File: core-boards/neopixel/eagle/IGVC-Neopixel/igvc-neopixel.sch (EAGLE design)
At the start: 21 parts, among them IC1 RT8289, IC2 ATMEGA8, X1 MSTBA2

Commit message: 11/17/19 I fixed the issues
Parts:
- removed ICSP: ICSP, pinhead:PINHD-2X3
- added ICSP1: ICSP, pinhead:PINHD-2X3
- added R5: 1M, SmartPrj:R-EU_R0603
- added R6: 27R, SmartPrj:R-EU_R0603
- added R7: 330, rcl:R-US_R0603
- added Y1: 16MHz, SmartPrj:RESONATORMU
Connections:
- new net N$1: JP1.2, R7.2
- new net XT1: R5.1, R6.2, Y1.3
- new net XT1R: IC2.XTAL1, R6.1
- new net XT2: IC2.XTAL2, R5.2, Y1.1
- net +5V: now also ICSP1.2; no longer ICSP.2
- net GND: now also ICSP1.6, Y1.2; no longer ICSP.6
- net LED_DATA: now also R7.1; no longer JP1.2
- net MISO: now also ICSP1.1; no longer ICSP.1
- net MOSI: now also ICSP1.4; no longer ICSP.4
- net RESET: now also ICSP1.5; no longer ICSP.5
- net SCK: now also ICSP1.3; no longer ICSP.3
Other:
- note added: "MISO"
- note added: "SCK"
- moved on the sheet: C6, JP1, JP2, R4, RESET

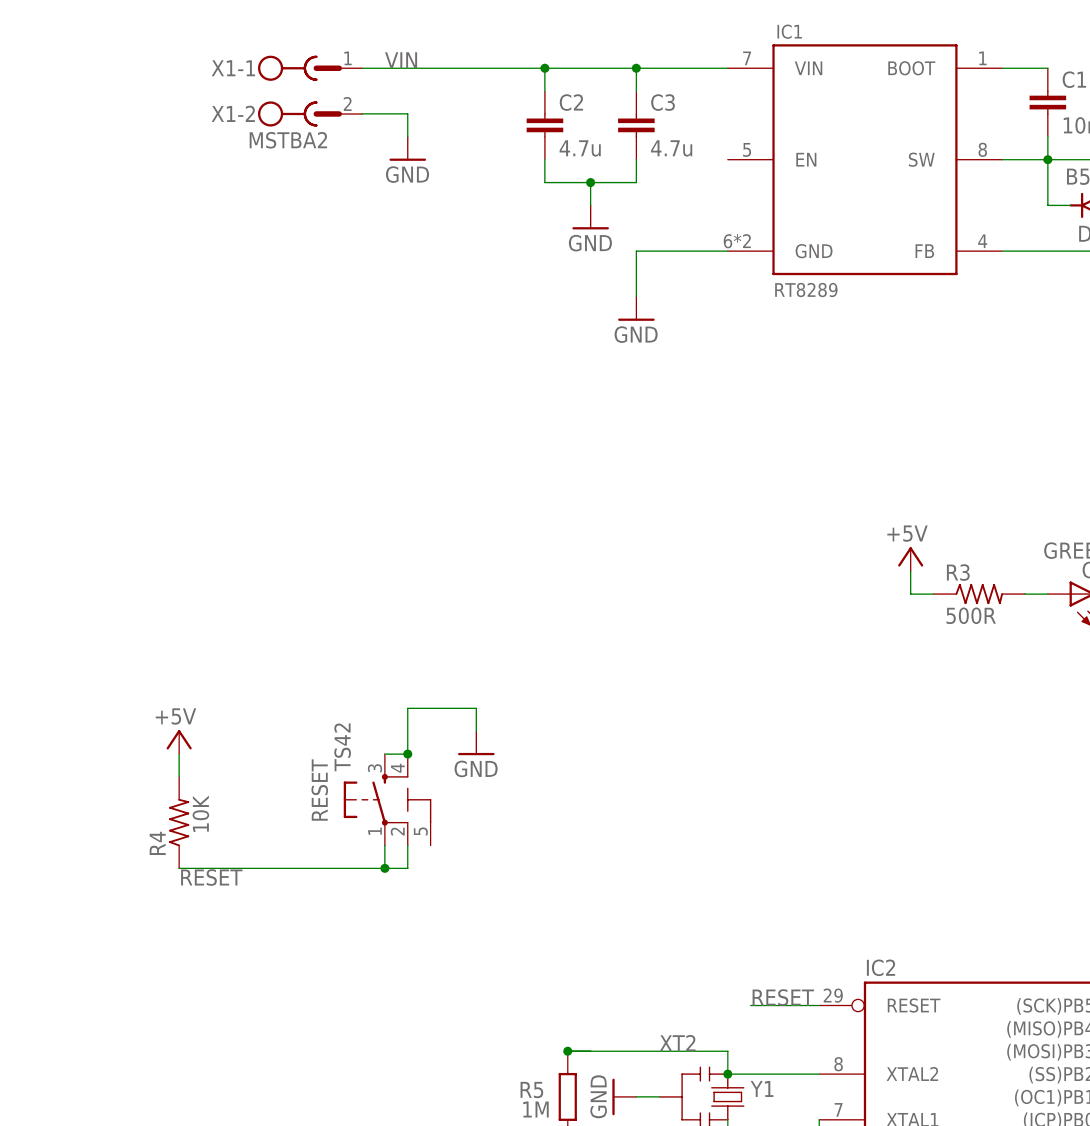
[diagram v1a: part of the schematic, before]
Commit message: Added Can Module (Inncomplete)
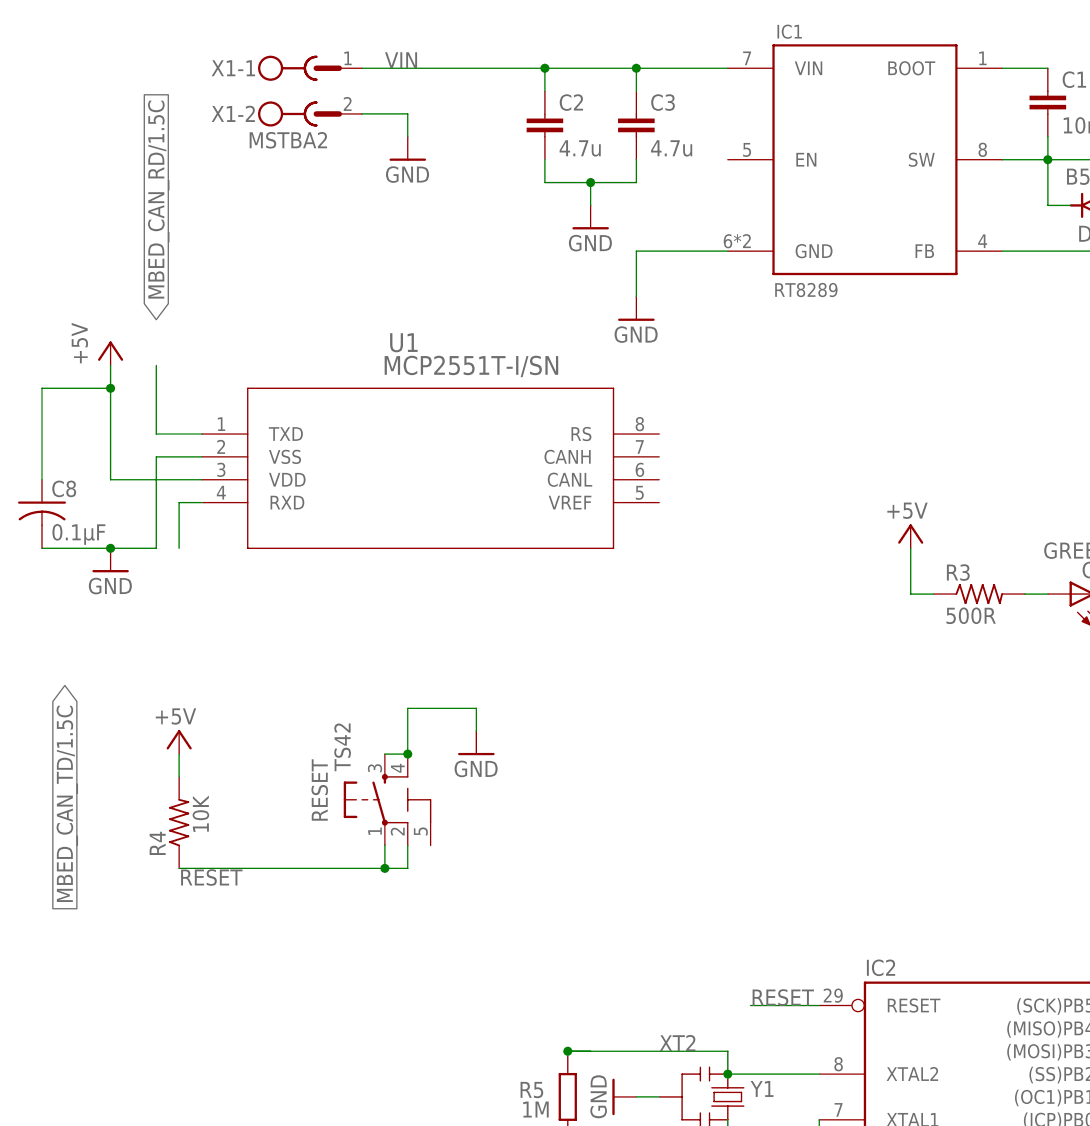
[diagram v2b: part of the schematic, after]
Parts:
- added C8: 0.1µF, adafruit:C-US025-024X044
- added U1: MCP2551T-I/SN, IGVC-Microcontroller:MCP2551T-I/SN
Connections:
- new net MBED_CAN_RD/1.5C: U1.TXD
- new net MBED_CAN_TD/1.5C: U1.RXD
- new net VCC: C8.1, U1.VDD
- net GND: now also C8.2, U1.VSS
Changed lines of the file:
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@@
 <?xml version="1.0" encoding="utf-8"?>
 <!DOCTYPE eagle SYSTEM "eagle.dtd">
-<eagle version="9.5.0">
+<eagle version="9.5.2">
 <drawing>
 <settings>
@@
 <part name="P+7" library="supply1" deviceset="+5V" device=""/>
 <part name="GND12" library="supply1" deviceset="GND" device=""/>
+<part name="U1" library="IGVC-Microcontroller" deviceset="MCP2551T-I/SN" device=""/>
+<part name="P+3" library="supply1" library_urn="urn:adsk.eagle:library:371" deviceset="VCC" device="" value="+5V"/>
+<part name="GND9" library="supply1" library_urn="urn:adsk.eagle:library:371" deviceset="GND" device=""/>
+<part name="C8" library="adafruit" library_urn="urn:adsk.eagle:library:420" deviceset="C-US" device="025-024X044" package3d_urn="urn:adsk.eagle:package:6240324/1" value="0.1µF"/>
 </parts>
 <sheets>
@@
 <attribute name="VALUE" x="20.32" y="68.58" size="1.778" layer="96" rot="R90"/>
 </instance>
-<instance part="P+2" gate="1" x="-10.16" y="76.2" smashed="yes">
-<attribute name="VALUE" x="-8.255" y="78.74" size="1.778" layer="96" rot="R180"/>
+<instance part="P+2" gate="1" x="-10.16" y="78.74" smashed="yes">
+<attribute name="VALUE" x="-8.255" y="81.28" size="1.778" layer="96" rot="R180"/>
 </instance>
 <instance part="C7" gate="G$1" x="-40.64" y="-7.62" smashed="yes" rot="MR180">
@@
 <instance part="GND12" gate="1" x="68.58" y="53.34" smashed="yes">
 <attribute name="VALUE" x="66.04" y="50.8" size="1.778" layer="96"/>
+</instance>
+<instance part="U1" gate="A" x="-91.44" y="88.9" smashed="yes">
+<attribute name="NAME" x="-68.2244" y="98.0186" size="2.0828" layer="95" ratio="6" rot="SR0"/>
+<attribute name="VALUE" x="-68.8594" y="95.4786" size="2.0828" layer="96" ratio="6" rot="SR0"/>
+</instance>
+<instance part="P+3" gate="VCC" x="-99.06" y="99.06" smashed="yes">
+<attribute name="VALUE" x="-101.6" y="96.52" size="1.778" layer="96" rot="R90"/>
+</instance>
+<instance part="GND9" gate="1" x="-99.06" y="73.66" smashed="yes">
+<attribute name="VALUE" x="-101.6" y="71.12" size="1.778" layer="96"/>
+</instance>
+<instance part="C8" gate="G$1" x="-106.68" y="81.28" smashed="yes">
+<attribute name="NAME" x="-105.664" y="81.915" size="1.778" layer="95"/>
+<attribute name="VALUE" x="-105.664" y="77.089" size="1.778" layer="96"/>
 </instance>
 </instances>
@@
 <segment>
 <wire x1="-7.62" y1="71.12" x2="-10.16" y2="71.12" width="0.1524" layer="91"/>
-<wire x1="-10.16" y1="71.12" x2="-10.16" y2="73.66" width="0.1524" layer="91"/>
+<wire x1="-10.16" y1="71.12" x2="-10.16" y2="76.2" width="0.1524" layer="91"/>
 <pinref part="P+2" gate="1" pin="+5V"/>
 <pinref part="R3" gate="G$1" pin="1"/>
@@
 <pinref part="ICSP1" gate="A" pin="6"/>
 </segment>
+<segment>
+<pinref part="GND9" gate="1" pin="GND"/>
+<wire x1="-99.06" y1="76.2" x2="-93.98" y2="76.2" width="0.1524" layer="91"/>
+<pinref part="U1" gate="A" pin="VSS"/>
+<wire x1="-93.98" y1="76.2" x2="-93.98" y2="86.36" width="0.1524" layer="91"/>
+<wire x1="-93.98" y1="86.36" x2="-88.9" y2="86.36" width="0.1524" layer="91"/>
+<wire x1="-99.06" y1="76.2" x2="-106.68" y2="76.2" width="0.1524" layer="91"/>
+<junction x="-99.06" y="76.2"/>
+<pinref part="C8" gate="G$1" pin="2"/>
+</segment>
 </net>
 <net name="RESET" class="0">
@@
 </segment>
 </net>
+<net name="VCC" class="0">
+<segment>
+<pinref part="P+3" gate="VCC" pin="VCC"/>
+<wire x1="-99.06" y1="96.52" x2="-99.06" y2="93.98" width="0.1524" layer="91"/>
+<pinref part="U1" gate="A" pin="VDD"/>
+<wire x1="-99.06" y1="93.98" x2="-99.06" y2="83.82" width="0.1524" layer="91"/>
+<wire x1="-99.06" y1="83.82" x2="-88.9" y2="83.82" width="0.1524" layer="91"/>
+<wire x1="-99.06" y1="93.98" x2="-106.68" y2="93.98" width="0.1524" layer="91"/>
+<junction x="-99.06" y="93.98"/>
+<wire x1="-106.68" y1="93.98" x2="-106.68" y2="83.82" width="0.1524" layer="91"/>
+<pinref part="C8" gate="G$1" pin="1"/>
+</segment>
+</net>
+<net name="MBED_CAN_RD/1.5C" class="0">
+<segment>
+<pinref part="U1" gate="A" pin="TXD"/>
+<wire x1="-88.9" y1="88.9" x2="-93.98" y2="88.9" width="0.1524" layer="91"/>
+<wire x1="-93.98" y1="88.9" x2="-93.98" y2="96.52" width="0.1524" layer="91"/>
+<label x="-93.98" y="101.6" size="1.778" layer="95" rot="R90" xref="yes"/>
+</segment>
+</net>
+<net name="MBED_CAN_TD/1.5C" class="0">
+<segment>
+<pinref part="U1" gate="A" pin="RXD"/>
+<wire x1="-88.9" y1="81.28" x2="-91.44" y2="81.28" width="0.1524" layer="91"/>
+<wire x1="-91.44" y1="81.28" x2="-91.44" y2="76.2" width="0.1524" layer="91"/>
+<label x="-104.14" y="60.96" size="1.778" layer="95" rot="R270" xref="yes"/>
+</segment>
+</net>

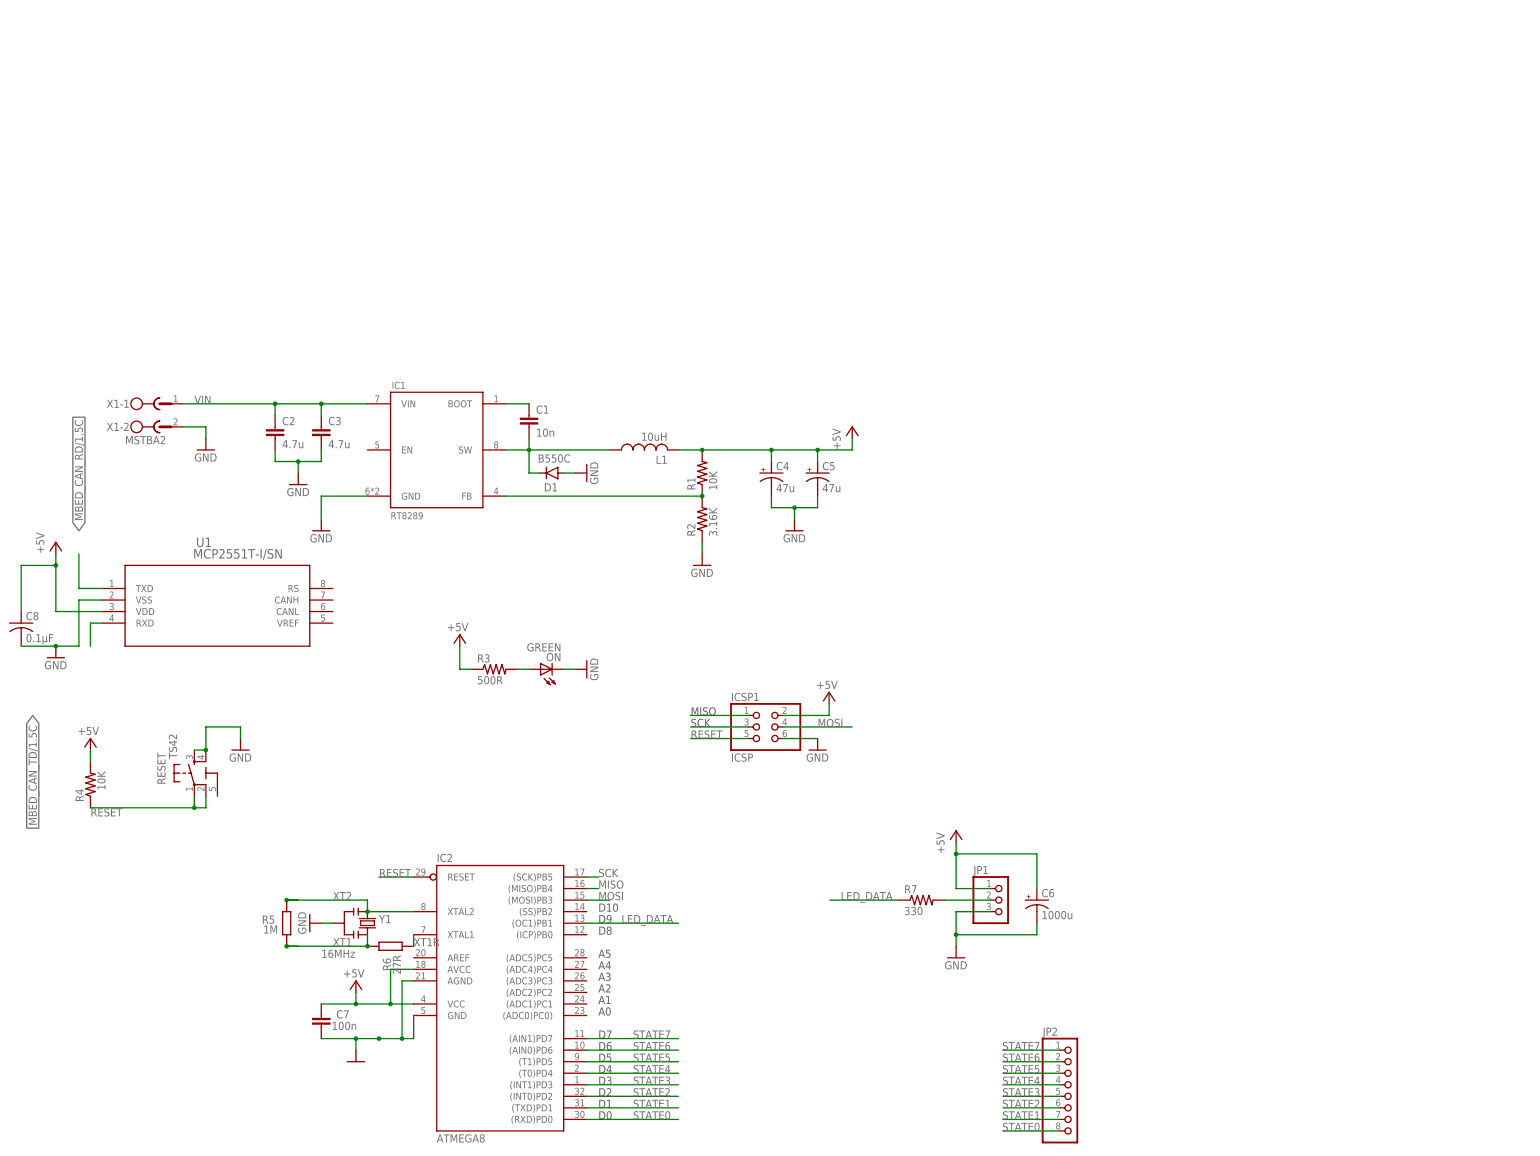
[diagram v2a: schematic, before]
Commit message: Relayout neopixel schematic
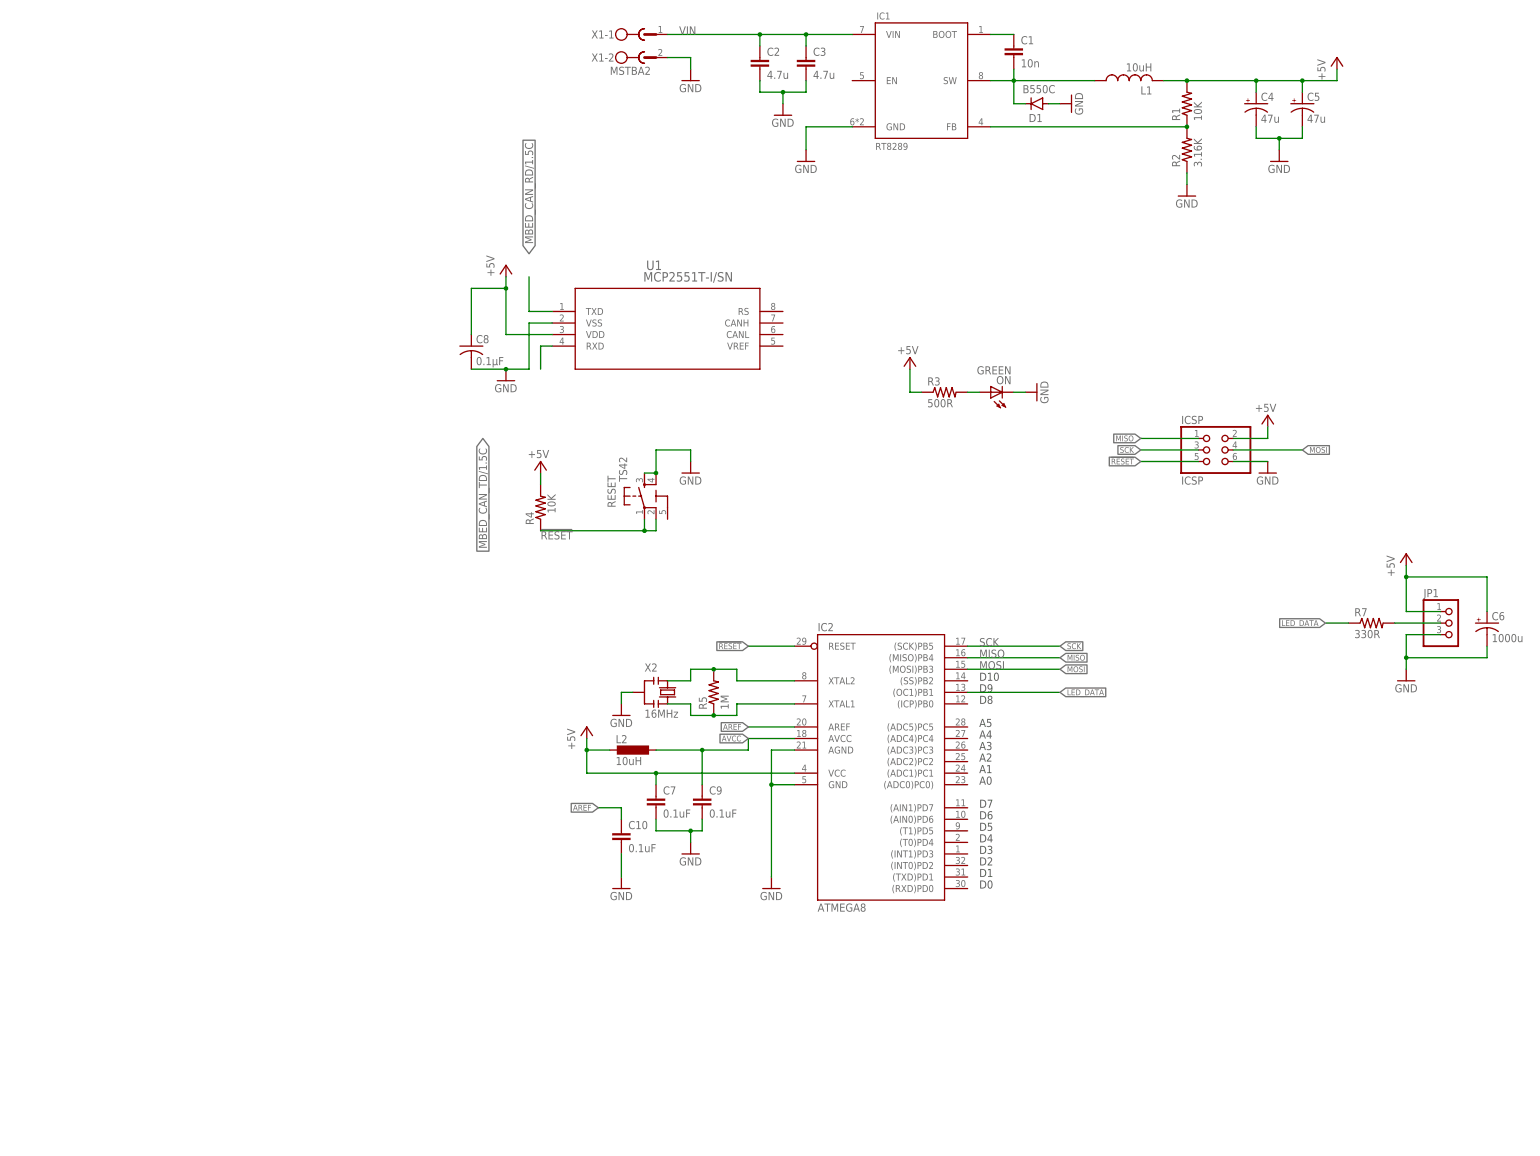
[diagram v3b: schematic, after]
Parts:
- removed ICSP1: ICSP, pinhead:PINHD-2X3
- removed JP2: (no value), pinhead:PINHD-1X8
- removed R6: 27R, SmartPrj:R-EU_R0603
- removed Y1: 16MHz, SmartPrj:RESONATORMU
- added C10, C9: 0.1uF, resistor:C-EUC0603
- added ICSP: ICSP, pinhead:PINHD-2X3
- added L2: 10uH, IGVC-Remote:L-0805
- added X2: 16MHz, IGVC-Remote:OSC_CSTCE16M0V53-R0
- C7: value 100n -> 0.1uF; device resistor:C-EUC0805 -> resistor:C-EUC0603
- R5: device SmartPrj:R-EU_R0603 -> resistor:R-US_R0603
- R7: value 330 -> 330R
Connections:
- removed net RESET: IC2.RESET, ICSP1.5, R4.1, RESET.1, RESET.2
- removed net STATE0: IC2.(RXD)PD0, JP2.8
- removed net STATE1: IC2.(TXD)PD1, JP2.7
- removed net STATE2: IC2.(INT0)PD2, JP2.6
- removed net STATE3: IC2.(INT1)PD3, JP2.5
- removed net STATE4: IC2.(T0)PD4, JP2.4
- removed net STATE5: IC2.(T1)PD5, JP2.3
- removed net STATE6: IC2.(AIN0)PD6, JP2.2
- removed net STATE7: IC2.(AIN1)PD7, JP2.1
- removed net XT1: R5.1, R6.2, Y1.3
- removed net XT1R: IC2.XTAL1, R6.1
- removed net XT2: IC2.XTAL2, R5.2, Y1.1
- new net !RESET: IC2.RESET, ICSP.5, R4.1, RESET.1, RESET.2
- new net AREF: C10.1, IC2.AREF
- new net AVCC: C9.1, IC2.AVCC, L2.1
- new net XTAL1: IC2.XTAL1, R5.1, X2.3
- new net XTAL2: IC2.XTAL2, R5.2, X2.1
- net +5V: now also C7.1, ICSP.2, L2.2; no longer C7.2, IC2.AVCC, ICSP1.2
- net GND: now also C10.2, C7.2, C9.2, ICSP.6, X2.2; no longer C7.1, ICSP1.6, Y1.2
- net MISO: now also ICSP.1; no longer ICSP1.1
- net MOSI: now also ICSP.4; no longer ICSP1.4
- net SCK: now also ICSP.3; no longer ICSP1.3
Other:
- note removed: "MISO"
- note removed: "SCK"
- moved on the sheet: C1, C2, C3, C4, C5, C6, C7, C8, D1, IC1, IC2, JP1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

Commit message: Finish relayout neopixel
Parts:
- removed C8: 0.1µF, adafruit:C-US025-024X044
- removed RESET: TS42, st-mod v1.4:TS42
- removed U1: MCP2551T-I/SN, IGVC-Microcontroller:MCP2551T-I/SN
- added C11: 22pF, resistor:C-EUC0603
- added D2, D3: RED, led:LEDCHIP-LED0805
- added J4: 4-PIN_2MM-H, RoboJackets-Connectors:4-PIN_2MM-H
- added R10, R9: 120R, rcl:R-US_R0603
- added R6, R8: 470R, resistor:R-US_R0603
- added SW1: SPST_TACT-EVQQ2, adafruit:SPST_TACT-EVQQ2
- added U$1: ROBOBUZZ1.0X, RoboJackets-Aesthetics:ROBOBUZZ1.0X
- added U3: MCP2551T-I/SN, MCP2551T:MCP2551T-I/SN
- R3: value 500R -> 470R; device resistor:R-US_R0805 -> resistor:R-US_R0603
- R4: device resistor:R-US_R0805 -> resistor:R-US_R0603
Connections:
- net L_ON renamed PWR_LED
- removed net VCC: C8.1, U1.VDD
- new net CAN_N/2.4A: J4.4, R10.1, R9.1, U3.CANL
- new net CAN_P/2.4A: J4.3, R10.2, R9.2, U3.CANH
- new net STAT1: IC2.(AIN1)PD7, R6.1
- new net STAT1_LED: D2.A, R6.2
- new net STAT2: IC2.(AIN0)PD6, R8.1
- new net STAT2_LED: D3.A, R8.2
- net !RESET: now also C11.2, SW1.S, SW1.S1; no longer RESET.1, RESET.2
- net +5V: now also J4.1, U3.VDD
- net GND: now also C11.1, D2.C, D3.C, J4.2, SW1.P, SW1.P1, U3.RS, U3.VSS; no longer C8.2, RESET.3, RESET.4, U1.VSS
- net MBED_CAN_RD/1.5C: now also IC2.(RXD)PD0, U3.TXD; no longer U1.TXD
- net MBED_CAN_TD/1.5C: now also IC2.(TXD)PD1, U3.RXD; no longer U1.RXD
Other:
- moved on the sheet: C1, C10, C2, C3, C4, C5, C6, C7, C9, D1, IC1, IC2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
